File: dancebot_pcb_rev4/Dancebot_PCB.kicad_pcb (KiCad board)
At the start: 2 copper layers, 66 x 53.3 mm, 64 parts, among them IC201 TPS63000IDRCRQ1, IC3 ESP32-S3-WROOM-1-N4, J12 USB_B_Micro, J13 Servo 4, J14 Servo 5, J2 Servo 1, J201 BatteryJ ST Connector, J3 Servo 2, J4 NeoPixel Left Eye, J7 Servo #, J9 NeoPixel Left Eye, Q1 IRLML6402TRPBF, SW1 RESET, SW2 BOOT, U1 IRLML2502TRPBF

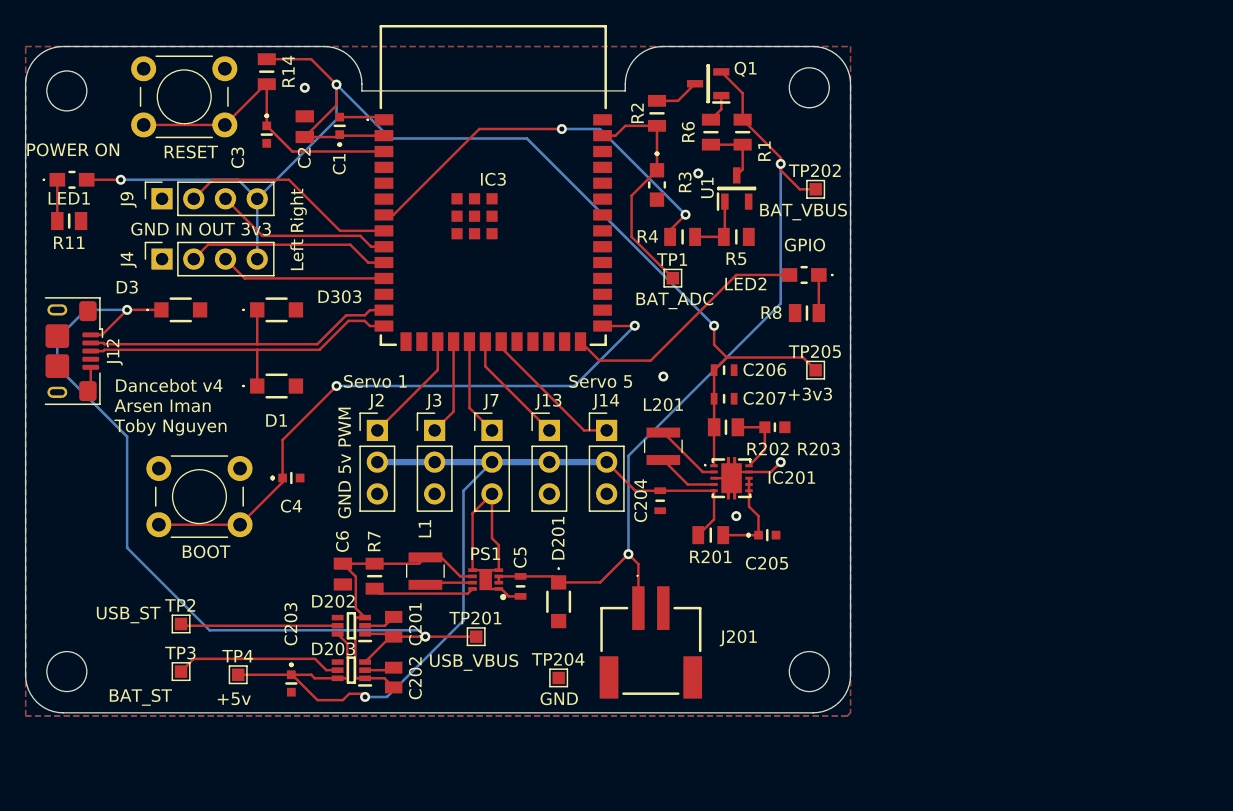
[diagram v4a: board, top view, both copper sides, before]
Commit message: added more power leds. need to finish routing. fixed 3d models
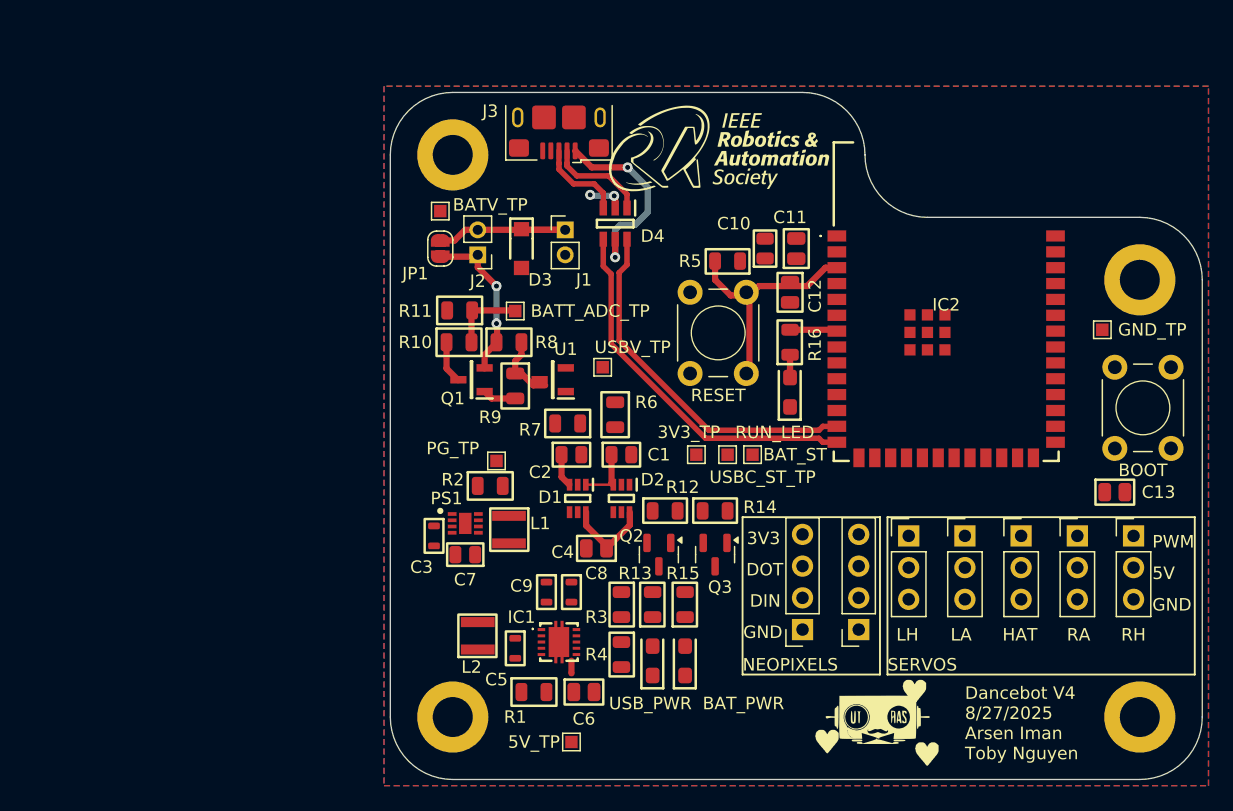
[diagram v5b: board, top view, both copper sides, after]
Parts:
- removed C201, C202: 1u, SamacSys_Parts:CAPC2012X135N
- removed C203, C205: 0.1u, SamacSys_Parts:MAJx16
- removed C204, C206, C207: 10u, SamacSys_Parts:CAPC1608X80N
- removed D201, D303: SMF5.0A_R1_00001, SamacSys_Parts:SMF50A_R1_00001
- removed D202, D203: LM66100DCKR, SamacSys_Parts:SOP65P210X110-6N
- removed H5: MountingHole_Pad, MountingHole:MountingHole_3.2mm_M3
- removed IC201: TPS63000IDRCRQ1, SamacSys_Parts:TPS63000IDRCRQ1
- removed IC3: ESP32-S3-WROOM-1-N4, SamacSys_Parts:ESP32S3WROOM1N4
- removed J12: USB_B_Micro, Connector_USB:USB_Micro-B_Amphenol_10118193-0002LF_Horizontal
- removed J13: Servo 4, Connector_PinHeader_2.54mm:PinHeader_1x03_P2.54mm_Vertical
- removed J14: Servo 5, Connector_PinHeader_2.54mm:PinHeader_1x03_P2.54mm_Vertical
- removed J201: BatteryJ ST Connector, SamacSys_Parts:1769
- removed L201: 2.2u, SamacSys_Parts:NRS3015T2R2MNGHV
- removed R201: 100, SamacSys_Parts:RESC2012X50N
- removed R202: 1M, SamacSys_Parts:RESC2012X60N
- removed R203: 200k, SamacSys_Parts:RESC1608X55N
- removed TP201: USBV, TestPoint:TestPoint_Pad_1.0x1.0mm
- removed TP202: BATV, TestPoint:TestPoint_Pad_1.0x1.0mm
- removed TP204: GND, TestPoint:TestPoint_Pad_1.0x1.0mm
- removed TP205: 3v3, TestPoint:TestPoint_Pad_1.0x1.0mm
- added C10: 22u, SamacSys_Parts:CAPC2012X145N, F.Cu at (142.0, 68.5)
- added C11: 0.1u, SamacSys_Parts:CAPC2012X140N, F.Cu at (144.5, 68.5)
- added C12: 0.1u, SamacSys_Parts:CAPC2012X140N, F.Cu at (144.0, 72.0)
- added C13: 0.1u, SamacSys_Parts:CAPC2012X140N, F.Cu at (170.0, 88.0)
- added C7: 22u, SamacSys_Parts:CAPC2012X145N, F.Cu at (118.0, 93.0)
- added C8: 10u, SamacSys_Parts:CAPC1608X80N, F.Cu at (126.5, 96.0)
- added C9: 10u, SamacSys_Parts:CAPC1608X80N, F.Cu at (124.5, 96.0)
- added D2: LM66100DCKR, SamacSys_Parts:SOP65P210X110-6N, F.Cu at (130.5, 88.5)
- added D4: USBLC6-4SC6Y, SamacSys_Parts:SOT95P280X145-6N, F.Cu at (130.0, 66.5)
- added G***: LOGO, LOGO, F.Cu at (154.0, 104.0)
- added G***: LOGO, LOGO, F.Cu at (151.0, 106.0)
- added G***: LOGO, LOGO, F.Cu at (138.5, 60.5)
- added G***: LOGO, LOGO, F.Cu at (147.0, 108.0)
- added G***: LOGO, LOGO, F.Cu at (155.0, 109.0)
- added H4: MountingHole_Pad, MountingHole:MountingHole_3.2mm_M3_ISO7380_Pad, F.Cu at (117.0, 61.0)
- added IC1: TPS63000IDRCRQ1, SamacSys_Parts:TPS63000IDRCRQ1, F.Cu at (125.5, 100.0)
- added IC2: ESP32-S3-WROOM-1-N4, SamacSys_Parts:ESP32S3WROOM1N4, F.Cu at (156.5, 73.0)
- added J1: BAT_IN, Connector_PinHeader_2.00mm:PinHeader_1x02_P2.00mm_Vertical, F.Cu at (126.0, 67.0)
- added J10: NeoPixel Left Eye, Connector_PinSocket_2.54mm:PinSocket_1x04_P2.54mm_Vertical, F.Cu at (145.0, 99.0)
- added J5: Servo 2, Connector_PinHeader_2.54mm:PinHeader_1x03_P2.54mm_Vertical, F.Cu at (158.0, 91.5)
- added J6: Servo 3, Connector_PinHeader_2.54mm:PinHeader_1x03_P2.54mm_Vertical, F.Cu at (162.5, 91.5)
- added J8: Servo 5, Connector_PinHeader_2.54mm:PinHeader_1x03_P2.54mm_Vertical, F.Cu at (171.5, 91.5)
- added JP1: Jumper_2_Bridged, Jumper:SolderJumper-2_P1.3mm_Open_RoundedPad1.0x1.5mm, F.Cu at (116.0, 68.5)
- added L2: 2.2u, SamacSys_Parts:NRS3015T2R2MNGHV, F.Cu at (119.0, 99.5)
- added LED3: APT2012PGW, SamacSys_Parts:APT2012PGW, F.Cu at (144.0, 80.0)
- added NT1: NetTie_2, NetTie:NetTie-2_SMD_Pad0.5mm, F.Cu at (126.5, 102.0)
- added Q2: IRLML6402TRPBF, Package_TO_SOT_SMD:SOT-23, F.Cu at (133.5, 93.0)
- added Q3: IRLML6402TRPBF, Package_TO_SOT_SMD:SOT-23, F.Cu at (138.0, 93.0)
- added R10: 100k, SamacSys_Parts:RESC2012X50N, F.Cu at (117.5, 76.0)
- added R12: 10k, SamacSys_Parts:RESC2012X60N, F.Cu at (134.0, 89.5)
- added R13: 1k, SamacSys_Parts:RESC2012X60N, F.Cu at (133.0, 97.0)
- added R15: 1k, SamacSys_Parts:RESC2012X60N, F.Cu at (135.6, 97.0)
- added R16: 1k, SamacSys_Parts:RESC2012X60N, F.Cu at (144.0, 76.0)
- added R9: 100, SamacSys_Parts:RESC2012X50N, F.Cu at (122.0, 79.5)
- added TP5: BATV_TP, SamacSys_Parts:TestPoint_Pad_1.0x1.0mm, F.Cu at (116.0, 65.5)
- added TP6: USBC_ST_TP, SamacSys_Parts:TestPoint_Pad_1.0x1.0mm, F.Cu at (139.0, 85.0)
- added TP7: BAT_ST, SamacSys_Parts:TestPoint_Pad_1.0x1.0mm, F.Cu at (141.0, 85.0)
- added TP8: PG_TP, SamacSys_Parts:TestPoint_Pad_1.0x1.0mm, F.Cu at (120.5, 85.5)
- added TP9: BATT_ADC_TP, SamacSys_Parts:TestPoint_Pad_1.0x1.0mm, F.Cu at (122.0, 73.5)
- C1: value 0.1u -> 1u; footprint SamacSys_Parts:MAJx16 -> SamacSys_Parts:CAPC2012X135N
- C2: value 22u -> 1u; footprint SamacSys_Parts:CAPC2012X145N -> SamacSys_Parts:CAPC2012X135N
- C3: value 0.1u -> 10u; footprint SamacSys_Parts:MAJx16 -> SamacSys_Parts:CAPC1608X80N
- C4: footprint SamacSys_Parts:MAJx16 -> SamacSys_Parts:CAPC2012X140N
- C6: value 22u -> 0.1u; footprint SamacSys_Parts:CAPC2012X145N -> SamacSys_Parts:CAPC2012X140N
- D1: value SMF5.0A_R1_00001 -> LM66100DCKR; footprint SamacSys_Parts:SMF50A_R1_00001 -> SamacSys_Parts:SOP65P210X110-6N
- H1, H2, H3: footprint MountingHole:MountingHole_3.2mm_M3 -> MountingHole:MountingHole_3.2mm_M3_ISO7380_Pad
- J2: value Servo 1 -> PWR_SW; footprint Connector_PinHeader_2.54mm:PinHeader_1x03_P2.54mm_Vertical -> Connector_PinHeader_2.00mm:PinHeader_1x02_P2.00mm_Vertical
- J3: value Servo 2 -> USB_B_Micro; footprint Connector_PinHeader_2.54mm:PinHeader_1x03_P2.54mm_Vertical -> Connector_USB:USB_Micro-B_Amphenol_10118193-0002LF_Horizontal
- J4: value NeoPixel Left Eye -> Servo 1; footprint Connector_PinSocket_2.54mm:PinSocket_1x04_P2.54mm_Vertical -> Connector_PinHeader_2.54mm:PinHeader_1x03_P2.54mm_Vertical
- J7: value Servo # -> Servo 4
- R1: value 100k -> 100
- R11: value 1k -> 51k; footprint SamacSys_Parts:RESC2012X60N -> SamacSys_Parts:ERA6AEB101V
- R14: footprint SamacSys_Parts:RESC2012X50N -> SamacSys_Parts:RESC2012X60N
- R3: value 51k -> 1M; footprint SamacSys_Parts:ERA6AEB101V -> SamacSys_Parts:RESC2012X60N
- R4: value 100 -> 200k; footprint SamacSys_Parts:RESC2012X50N -> SamacSys_Parts:RESC2012X60N
- R5: value 100k -> 10k; footprint SamacSys_Parts:RESC2012X50N -> SamacSys_Parts:RESC2012X60N
- R8: value 1k -> 100k; footprint SamacSys_Parts:RESC2012X60N -> SamacSys_Parts:RESC2012X50N
- TP1: value BATT_ADC -> GND_TP; footprint TestPoint:TestPoint_Pad_1.0x1.0mm -> SamacSys_Parts:TestPoint_Pad_1.0x1.0mm
- TP2: value USBC_ST -> 3V3_TP; footprint TestPoint:TestPoint_Pad_1.0x1.0mm -> SamacSys_Parts:TestPoint_Pad_1.0x1.0mm
- TP3: value BAT_ST -> 5V_TP; footprint TestPoint:TestPoint_Pad_1.0x1.0mm -> SamacSys_Parts:TestPoint_Pad_1.0x1.0mm
- TP4: value 5v -> USBV_TP; footprint TestPoint:TestPoint_Pad_1.0x1.0mm -> SamacSys_Parts:TestPoint_Pad_1.0x1.0mm
- moved H1 87.2 mm to (172.0, 71.0)
- moved SW2 81.4 mm to (174.5, 78.0), turned to -90 degrees
- moved J9 65.6 mm to (149.5, 99.0), turned to 180 degrees
- moved J4 63.7 mm to (153.5, 91.5), turned to 0 degrees
- moved LED1 60.4 mm to (133.0, 101.5), turned to 90 degrees
- moved H3 56.9 mm to (172.0, 106.0)
- moved R14 50.2 mm to (138.0, 89.5), turned to 0 degrees
- moved SW1 50.1 mm to (136.0, 78.5), turned to 90 degrees
- moved R1 47.8 mm to (123.5, 104.0), turned to 0 degrees
- moved J7 47.6 mm to (167.0, 91.5)
- moved TP2 43.4 mm to (136.5, 85.0), turned to 180 degrees
- moved TP4 38.2 mm to (129.0, 78.0)
- moved C3 34.8 mm to (115.5, 91.5)
- moved C1 34.7 mm to (130.5, 85.0), turned to 0 degrees
- moved TP1 34.6 mm to (169.0, 75.0), turned to 180 degrees
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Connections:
- net Net-(PS1-SW) renamed /POWER/SW0
- C1 pad 1: +3V3 -> /POWER/USB_VBUS
- C2 pad 1: +3V3 -> /POWER/STEP_VBUS
- C3 pad 1: /MCU/EN -> /BATTERY_STAT/BAT_VBUS2
- C4 pad 1: /MCU/IO0 -> +5V
- C5 pad 1: /BATTERY_STAT/BAT_VBUS -> +5V
- C5 pad 2: GND -> GNDPWR
- C6 pad 1: Net-(D202-~{CE}) -> /POWER/TPS_IN
- D1 pad 1: /MCU/D+ -> /POWER/USB_VBUS
- D3 pad 1: /POWER/USB_VBUS -> /POWER/BAT_VBUS1
- J2 pad 1: /MCU/SM1 -> /BATTERY_STAT/BAT_VBUS2
- J2 pad 2: +5V -> /POWER/BAT_VBUS1
- J3 pad 1: /MCU/SM2 -> /POWER/USB_VBUS
- J3 pad 2: +5V -> /USB_MICRO/USBD-
- J3 pad 3: GND -> /USB_MICRO/USBD+
- J4 pad 1: GND -> /MCU/SM.LH
- J4 pad 2: /LEDS/NP2_DIN -> +5V
- J4 pad 3: /LEDS/NP2_DOUT -> GND
- J7 pad 1: /MCU/SM3 -> /MCU/SM.RA
- L1 pad 2: Net-(D202-~{CE}) -> /POWER/STEP_VBUS
- LED1 pad 1: Net-(LED1-K) -> GND
- LED1 pad 2: +3V3 -> Net-(LED1-A)
- LED2 pad 1: Net-(LED2-K) -> GND
- LED2 pad 2: /LEDS/IO45 -> Net-(LED2-A)
- PS1 pad 2: /BATTERY_STAT/BAT_VBUS -> /BATTERY_STAT/BAT_VBUS2
- PS1 pad 3: /BATTERY_STAT/BAT_VBUS -> /BATTERY_STAT/BAT_VBUS2
- PS1 pad 6: Net-(D202-~{CE}) -> /POWER/STEP_VBUS
- Q1 pad 1: Net-(Q1-Pad1) -> /BATTERY_STAT/PMOS_GATE
- Q1 pad 2: /BATTERY_STAT/BAT_VBUS -> /BATTERY_STAT/BAT_VBUS2
- Q1 pad 3: Net-(Q1-Pad3) -> /BATTERY_STAT/PMOS_SOURCE
- R1 pad 1: /BATTERY_STAT/BAT_VBUS -> +5V
- R1 pad 2: Net-(R1-Pad2) -> /POWER/TPS_IN
- R11 pad 1: Net-(LED1-K) -> /BATTERY_STAT/BATT_ADC
- R14 pad 2: /MCU/EN -> /LEDS/USBC_ST
- R2 pad 1: Net-(Q1-Pad3) -> Net-(PS1-PG)
- R2 pad 2: /BATTERY_STAT/BATT_ADC -> /POWER/STEP_VBUS
- R3 pad 1: /BATTERY_STAT/BATT_ADC -> +3V3
- R3 pad 2: GND -> /POWER/FB
- R4 pad 1: /BATTERY_STAT/BATT_EN -> /POWER/FB
- R4 pad 2: Net-(R4-Pad2) -> GND
- R5 pad 1: Net-(R4-Pad2) -> +3V3
- R5 pad 2: GND -> /MCU/EN
- R6 pad 1: Net-(R1-Pad2) -> /BATTERY_STAT/BATT_ADC_EN
- R6 pad 2: Net-(Q1-Pad1) -> /BATTERY_STAT/NMOS_GATE
- R7 pad 1: Net-(PS1-PG) -> /BATTERY_STAT/NMOS_GATE
- R7 pad 2: Net-(D202-~{CE}) -> GND
- R8 pad 1: Net-(LED2-K) -> /BATTERY_STAT/BAT_VBUS2
- R8 pad 2: GND -> /BATTERY_STAT/NMOS_DRAIN
- TP1 pad 1: /BATTERY_STAT/BATT_ADC -> GND
- TP2 pad 1: /POWER/USBC_ST -> +3V3
- TP3 pad 1: /POWER/BAT_ST -> +5V
- TP4 pad 1: +5V -> /POWER/USB_VBUS
- U1 pad 1: Net-(R4-Pad2) -> /BATTERY_STAT/NMOS_GATE
- U1 pad 3: Net-(R1-Pad2) -> /BATTERY_STAT/NMOS_DRAIN
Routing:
- net +3V3: track 106.8 -> 0.00 mm, vias 3 -> 0
- net +5V: track 75.7 -> 7.25 mm, vias 1 -> 0
- net /BATTERY_STAT/BAT_VBUS: track 66.2 -> 0.00 mm, vias 2 -> 0
- net /MCU/IO0: track 49.3 -> 0.00 mm, vias 2 -> 0
- net /POWER/USB_VBUS: track 68.3 -> 20.5 mm
- net GND: track 35.8 -> 2.96 mm, vias 5 -> 2
- net /BATTERY_STAT/BATT_EN: track 32.1 -> 0.00 mm, vias 2 -> 0
- net Net-(D202-~{CE}): track 25.1 -> 0.00 mm
- net /LEDS/IO45: track 20.2 -> 0.00 mm
- net /LEDS/NP1_DIN: track 17.6 -> 0.00 mm
- net /LEDS/NP2_DIN: track 16.3 -> 0.00 mm
- net /LEDS/NP1_DOUT: track 14.3 -> 0.00 mm
- net /POWER/BAT_VBUS1: track 0.00 -> 13.9 mm
- net /POWER/BAT_ST: track 13.3 -> 0.00 mm
- net /LEDS/NP2_DOUT: track 13.3 -> 0.00 mm
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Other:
- board size 66 x 53.3 mm -> 65 x 55 mm
- board text added: "3V3"
- board text added: "5V"
- board text added: "5V power ORring"
- board text added: "5V to 3V"
- board text added: "BAT reader"
- board text added: "BAT to 5V"
- board text added: "BAT_PWR"
- board text added: "DIN"
- board text added: "DOT"
- board text added: "Dancebot V4 8/27/2025 Arsen Iman Toby Nguyen"
- board text added: "H - Hip, A - Ankle (i.e. LH -> Left Hip)"
- board text added: "HAT"
- board text added: "LA"
- board text added: "LED power indicator"
- board text added: "LH"
- board text added: "NEOPIXELS"
- board text added: "Not possible to route USB data lines over solid ref plane because of D+/D- location on ESP32 module"
- board text added: "PWM"
- board text added: "RA"
- board text added: "RH"
- board text added: "RUN_LED"
- board text added: "SERVOS"
- board text added: "USB_PWR"
- board text added: "battery"
- board text removed: "+3v3"
- board text removed: "+5v"
- board text removed: "BAT_ADC"
- board text removed: "BAT_ST"
- board text removed: "BAT_VBUS"
- board text removed: "Dancebot v4 Arsen Iman Toby Nguyen"
- board text removed: "GND 5v PWM"
- board text removed: "GND IN OUT 3v3"
- board text removed: "GPIO"
- board text removed: "Left Right"
- board text removed: "POWER ON"
- board text removed: "Servo 1"
- board text removed: "Servo 5"
- board text removed: "USB_ST"
- board text removed: "USB_VBUS"

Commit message: finished first layout. need to add polygon pours
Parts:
- J10: value NeoPixel Left Eye -> NeoPixel Right Eye
- NT1: footprint NetTie:NetTie-2_SMD_Pad0.5mm -> SamacSys_Parts:NetTie-2_SMD_Pad0.3mm
- TP2: value 3V3_TP -> 3.3TP
- TP7: value BAT_ST -> BAT_ST_TP
- moved TP2 13.1 mm to (137.2, 98.1), turned to 0 degrees
- moved J10 4.50 mm to (149.5, 99.0)
- moved J9 4.50 mm to (145.0, 99.0)
- moved NT1 2.52 mm to (126.2, 99.5), turned to 180 degrees
- moved TP7 1.58 mm to (142.5, 85.5)
- moved TP6 1.12 mm to (138.0, 85.5), turned to 180 degrees
- moved C13 1.00 mm to (171.0, 88.0)
- moved G*** 0.79 mm to (153.2, 103.8)
- moved LED2 0.60 mm to (135.0, 101.5)
- moved R15 0.60 mm to (135.0, 97.0)
- moved G*** 0.59 mm to (154.5, 109.3)
- moved Q3 0.55 mm to (134.1, 93.0)
- moved G*** 0.50 mm to (151.0, 106.5)
- moved G*** 0.50 mm to (147.0, 108.5)
- moved LED1 0.50 mm to (132.5, 101.5)
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- renumbered U1 to Q1, Q1 to Q2, Q2 to Q3, Q3 to Q4
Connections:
- IC2 pad 4: /BATTERY_STAT/BATT_ADC_EN -> unconnected-(IC2-IO4-Pad4)
- J10 pad 2: /LEDS/NP2_DIN -> +3V3
- J10 pad 4: +3V3 -> /LEDS/NP2_DIN
- J9 pad 2: /LEDS/NP1_DIN -> +3V3
- J9 pad 4: +3V3 -> /LEDS/NP1_DIN
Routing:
- net +3V3: track 0.00 -> 93.5 mm, vias 0 -> 6
- net +5V: track 7.25 -> 91.0 mm, vias 0 -> 3
- net /BATTERY_STAT/BATT_ADC: track 6.04 -> 35.1 mm, vias 0 -> 2
- net /POWER/STEP_VBUS: track 2.65 -> 30.8 mm, vias 0 -> 2
- net /LEDS/USBC_ST: track 0.00 -> 26.0 mm
- net /BATTERY_STAT/BATT_ADC_EN: track 0.00 -> 25.5 mm, vias 0 -> 2
- net /LEDS/BAT_ST: track 0.00 -> 23.8 mm, vias 0 -> 2
- net /POWER/USB_VBUS: track 20.5 -> 41.1 mm, vias 2 -> 0
- net /BATTERY_STAT/BAT_VBUS2: track 13.2 -> 30.8 mm, vias 2 -> 4
- net /MCU/IO0: track 0.00 -> 17.1 mm
- net /LEDS/NP1_DOUT: track 0.00 -> 13.2 mm
- net GND: track 2.96 -> 15.9 mm, vias 2 -> 83
- net /MCU/SM.RH: track 0.00 -> 12.5 mm
- net /LEDS/NP2_DOUT: track 0.00 -> 11.3 mm
- net GNDPWR: track 0.00 -> 10.8 mm, vias 0 -> 2
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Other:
- board text added: "Antenna Keepout"

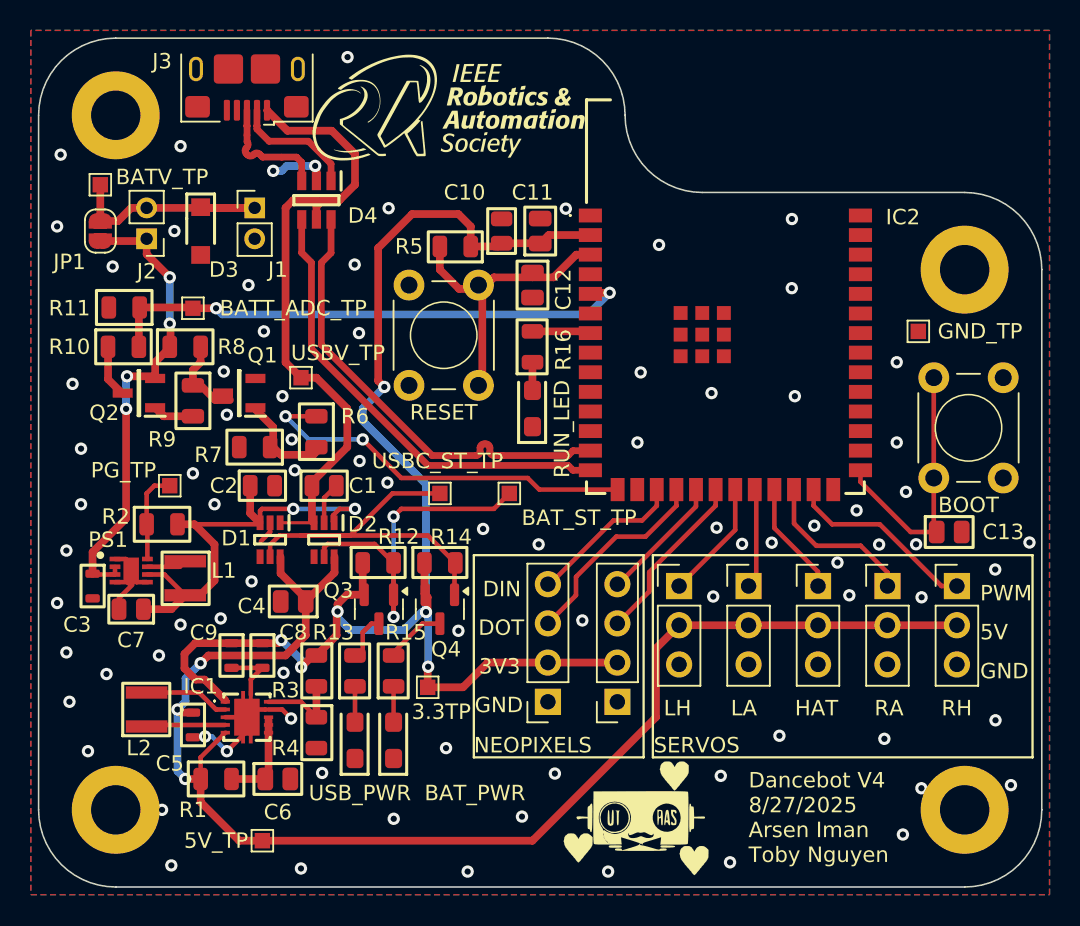
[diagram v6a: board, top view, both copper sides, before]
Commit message: moved some more stuff around. added gerbers
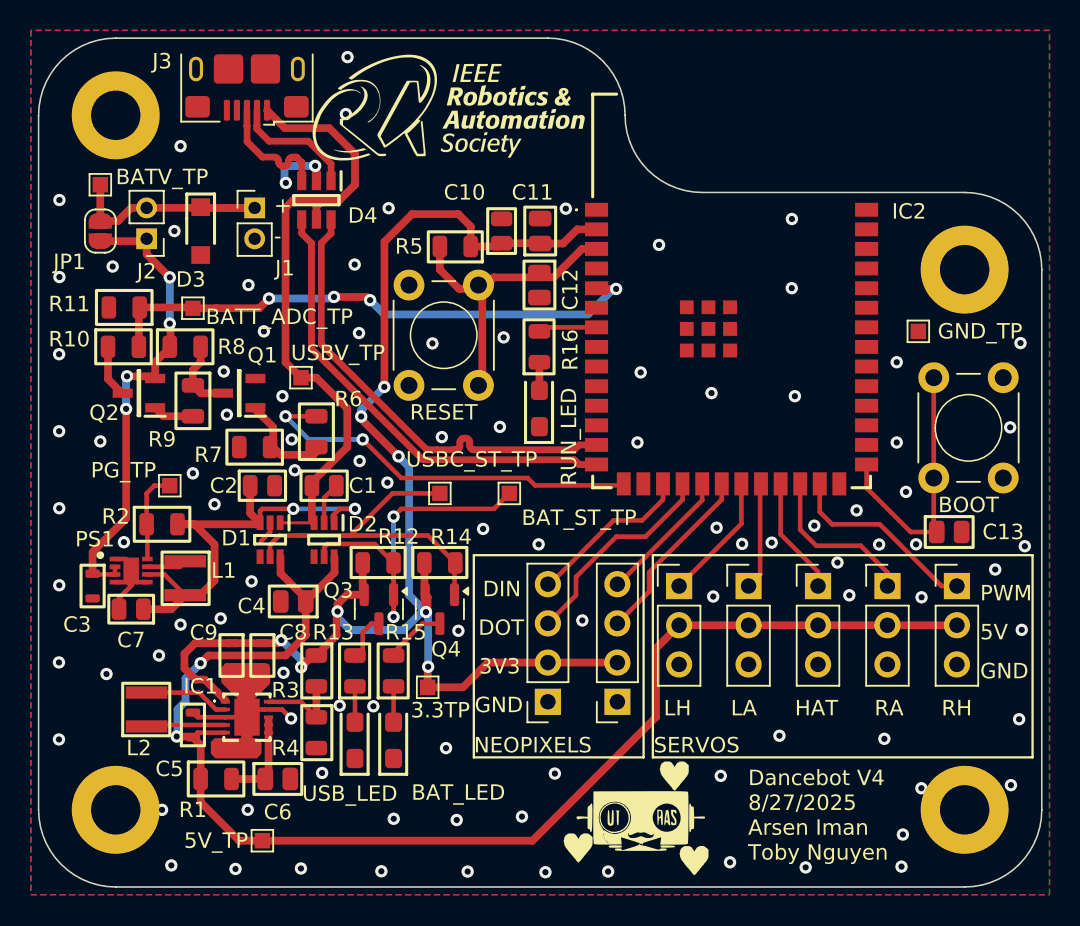
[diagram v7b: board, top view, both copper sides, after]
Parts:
- added G***: LOGO, LOGO, B.Cu at (143.9, 86.4)
- moved IC2 0.54 mm to (156.9, 72.6)
- moved C12 0.45 mm to (144.4, 72.0)
- moved LED3 0.45 mm to (144.4, 80.0)
- moved R16 0.45 mm to (144.4, 76.0)
- turned C5 to 90 degrees
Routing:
- net GNDPWR: track 10.8 -> 3.62 mm, vias 2 -> 0
- net +5V: track 91.0 -> 88.5 mm, vias 3 -> 2
- net /BATTERY_STAT/BATT_ADC: track 35.1 -> 36.2 mm, vias 2 -> 4
- net /BATTERY_STAT/NMOS_DRAIN: track 5.50 -> 4.86 mm
- net /MCU/EN: track 19.2 -> 19.7 mm
- net /MCU/SM.LH: track 7.76 -> 8.29 mm
- net /LEDS/NP2_DIN: track 8.27 -> 8.81 mm
- net /LEDS/NP1_DIN: track 10.2 -> 10.7 mm
- net /LEDS/NP1_DOUT: track 13.2 -> 13.8 mm
- net /LEDS/NP2_DOUT: track 11.3 -> 11.8 mm
- net +3V3: track 93.5 -> 93.8 mm, vias 6 -> 8
- net GND: track 15.9 -> 16.0 mm, vias 83 -> 100
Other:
- board text added: "+"
- board text added: "-"
- board text added: "BAT_LED"
- board text added: "USB_LED"
- board text added: "Your ability to nap will soon be legendary :)"
- board text removed: "BAT_PWR"
- board text removed: "USB_PWR"
